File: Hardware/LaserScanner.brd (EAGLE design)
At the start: 160 x 100 mm, 84 parts, among them J1 USB, J2 !KILL!, J3 KEYSWITCH, J5 ESTOP, J8 Power Input, Q1 MBT3904DW1T1, Q4 2.5A/30V/105mΩ, U1 ESP-WROOM-32, U2 3.3V, U3 CH340C

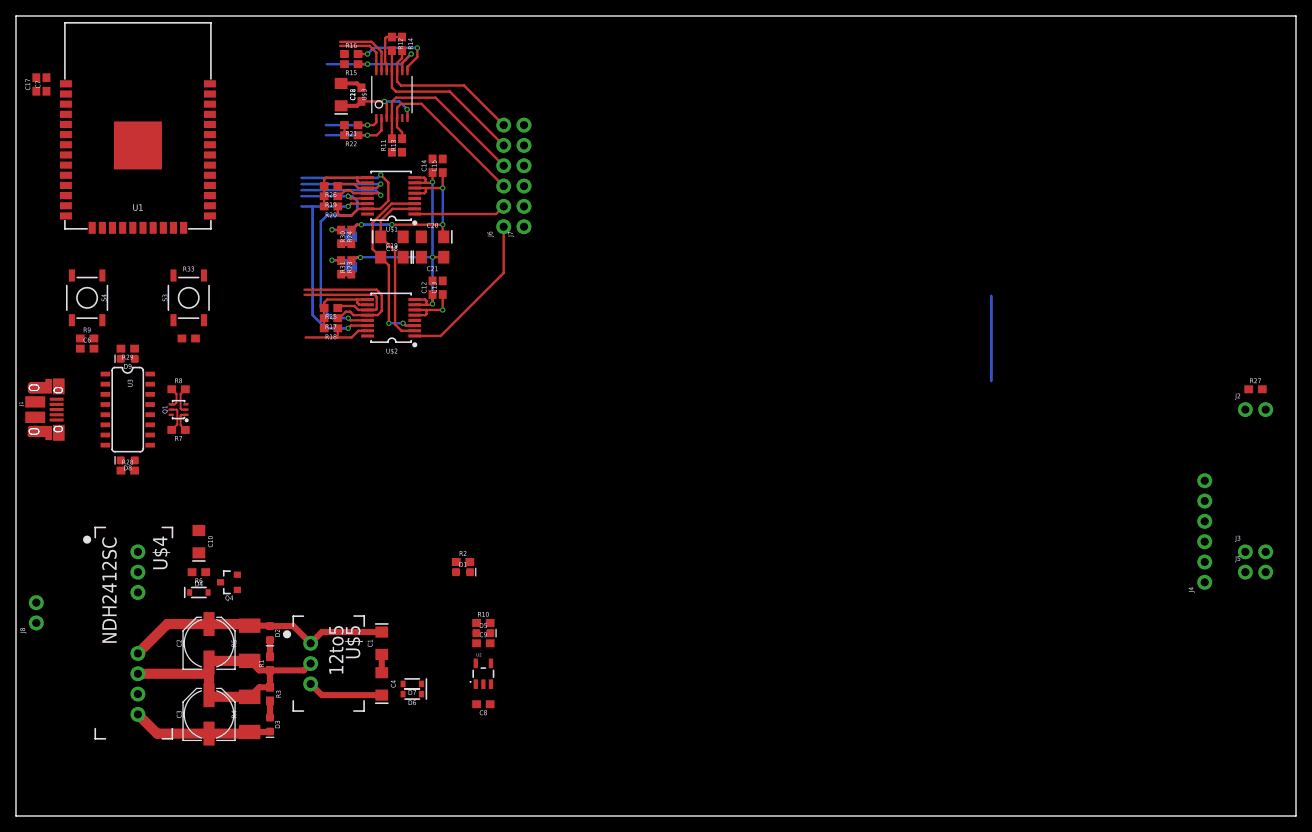
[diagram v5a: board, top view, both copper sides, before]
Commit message: Added silk, optimized ground planes, and cammed
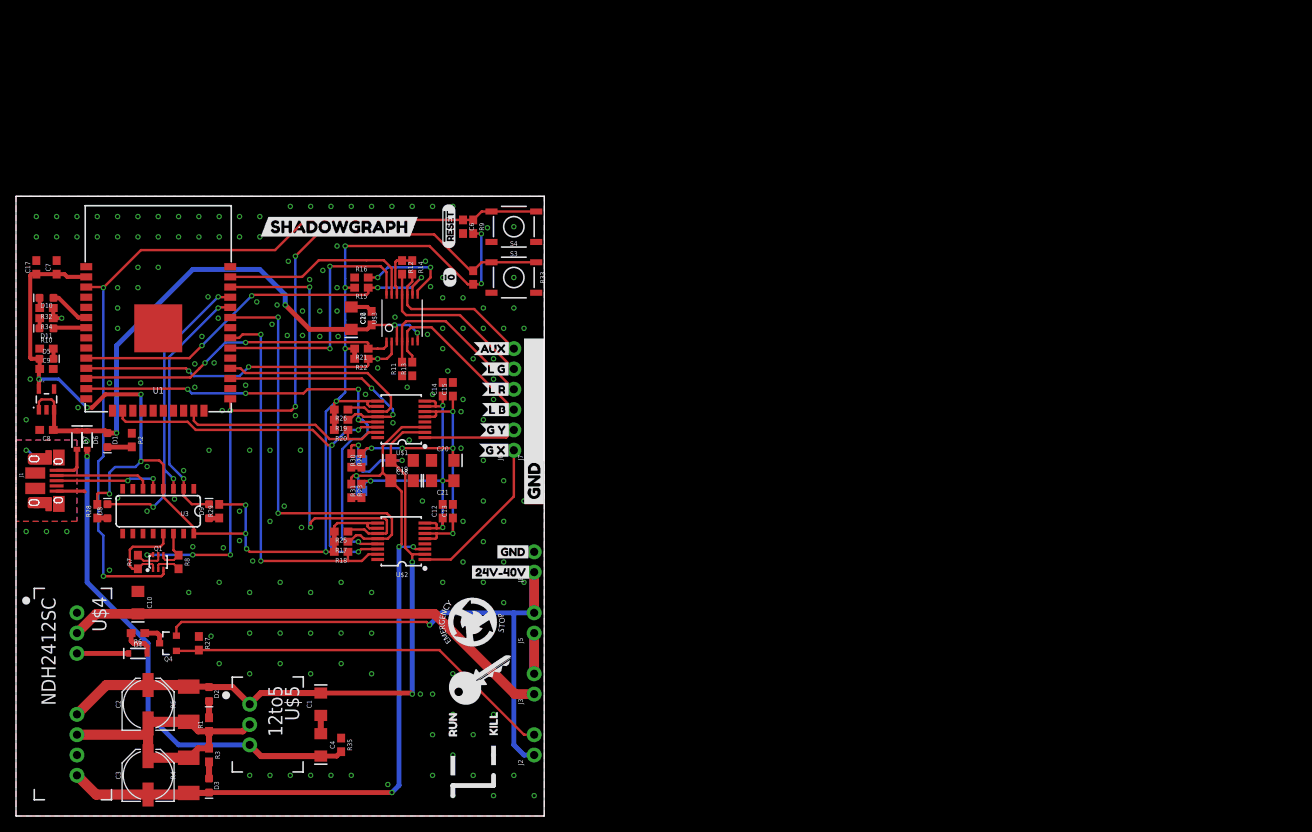
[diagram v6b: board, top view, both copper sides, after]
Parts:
- removed J4: (no value), SparkFun-Connectors:1X06_NO_SILK
- added D10, D11: BLUE, SparkFun-LED:LED-0603
- added R32, R34: 1k, SparkFun-Resistors:0603
- added R35: 100, SparkFun-Resistors:0603
- added U$10: (no value), buzzard_labels:GND1
- added U$11: (no value), buzzard_labels:KILL11
- added U$12: (no value), buzzard_labels:RUN10
- added U$13: (no value), buzzard_labels:#RESET14
- added U$14: (no value), buzzard_labels:#013
- added U$15: (no value), buzzard_labels:AUX4
- added U$16: (no value), buzzard_labels:G_X14
- added U$17: (no value), buzzard_labels:G_Y13
- added U$18: (no value), buzzard_labels:L_B12
- added U$19: (no value), buzzard_labels:LPF_BYPASS12
- added U$20: (no value), buzzard_labels:L_R14
- added U$21: (no value), buzzard_labels:L_G10
- added U$22: (no value), buzzard_labels:SHADOWGRAPH15
- added U$6: (no value), key#png:KEY#PNG
- added U$7: (no value), e#stop#jpg:E#STOP#JPG
- added U$8: (no value), buzzard_labels:24V#40V3
- added U$9: (no value), buzzard_labels:GND0
- moved R27 135.8 mm to (22.9, 21.6), turned to 270 degrees
- moved J2 98.8 mm to (64.8, 7.62), turned to 90 degrees
- moved J3 90.7 mm to (64.8, 15.2), turned to 90 degrees
- moved J5 89.2 mm to (64.8, 22.9), turned to 90 degrees
- moved C9 64.5 mm to (3.81, 55.9)
- moved R10 64.5 mm to (3.81, 58.4)
- moved C8 64.5 mm to (3.81, 48.3)
- moved D5 64.5 mm to (3.81, 57.1)
- moved U2 64.5 mm to (3.81, 52.1)
- moved J8 62.6 mm to (64.8, 30.5)
- moved S4 54.1 mm to (62.2, 73.7), turned to 0 degrees
- moved D7 51.8 mm to (7.62, 47.0), turned to 270 degrees
- moved D6 51.6 mm to (8.89, 47.0), turned to 270 degrees
- moved R9 50.2 mm to (57.1, 73.7), turned to 270 degrees
- moved C6 49.4 mm to (55.9, 73.7), turned to 270 degrees
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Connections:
- removed net N$24: U1.6
- removed net N$25: U1.7
- new net N$17: D10.C, R32.2
- new net N$18: D11.C, R34.2
- new net ULED1: D10.A, U1.6
- new net ULED2: D11.A, U1.7
- net GND: now also R32.1, R34.1, R35.1; no longer J4.1, J4.2, J4.3, J4.4, J4.5, J4.6
- net N$7: now also R35.2
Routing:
- net 3.3V: track 22.5 -> 187.1 mm, vias 0 -> 15
- net RESET: track 0.00 -> 105.5 mm, vias 0 -> 2
- net 0: track 0.00 -> 91.4 mm, vias 0 -> 6
- net VCC: track 0.00 -> 76.6 mm, vias 0 -> 1
- net 5V: track 12.2 -> 75.3 mm, vias 2 -> 4
- net VCC_SWITCHED: track 0.00 -> 62.3 mm
- net -12V: track 44.5 -> 101.8 mm, vias 3 -> 4
- net N$7: track 9.47 -> 62.8 mm, vias 0 -> 1
- net !KILL: track 0.00 -> 49.1 mm
- net GX_!RST: track 15.9 -> 57.3 mm, vias 0 -> 2
- net TXO: track 0.00 -> 39.9 mm, vias 0 -> 3
- net GX_!LDAC: track 9.25 -> 48.4 mm, vias 0 -> 2
- net 12V: track 58.9 -> 96.2 mm, vias 1 -> 4
- net GX_!CS: track 18.2 -> 53.3 mm, vias 0 -> 2
- net L_!CLR: track 14.9 -> 49.1 mm, vias 2 -> 4
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- added copper zone on layer 1, net GND
- added copper zone on layer 16, net GND
- added copper zone on layer 1, net SHIELD
- added copper zone on layer 16, net SHIELD
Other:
- board size 160 x 100 mm -> 66 x 77.5 mm

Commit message: add failsafes to schematic
failsafes include:
- pulling the laser dac clr line to gnd if kill_n goes low or if VCC is interrupted (can be used to safe the laser)
- disabling the 3.3V rail (effectively stopping laser output and microcontroller) when kill_n or VCC go low (allowing external kill and interlocks to make safe even when USB is powering 5V rail)

todo: routing
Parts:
- added Q2, Q5: 3.1A/30V/105mΩ, SparkFun-DiscreteSemi:SOT23-3
- added Q3, Q6, Q7, Q8: 5.8A/30V/35mΩ, SparkFun-DiscreteSemi:SOT23-3
- added R36, R37, R39: 10k, SparkFun-Resistors:0603
- Q4: value 2.5A/30V/105mΩ -> 3.1A/30V/105mΩ
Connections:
- new net 3V3_EN: Q7.2, R39.2, U2.3
- new net N$19: Q2.3, Q3.1, R36.2
- new net N$20: Q5.3, Q6.1, R37.2
- new net N$21: Q7.3, Q8.2
- net !KILL: now also Q2.1, Q7.1
- net 3.3V: now also Q5.2
- net 5V: now also Q8.3; no longer U2.3
- net GND: now also Q3.2, Q6.2, R36.1, R37.1, R39.1
- net L_!CLR: now also Q3.3, Q6.3
- net VCC: now also Q2.2, Q5.1, Q8.1
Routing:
- net 5V: track 75.3 -> 71.9 mm
